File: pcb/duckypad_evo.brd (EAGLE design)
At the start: 90 x 96 mm, 93 parts, among them IC1 STM32F072C8T6, IC2 REG1117, IC3 74AHCT1G08DBV, SW1 324_SW324_SWITCH_FOOT_HOLE, SW10 KAILH_SWITCH_SOCKET_KAILH_SWI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, SW11 KAILH_SWITCH_SOCKET_KAILH_SWI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, SW12 KAILH_SWITCH_SOCKET_KAILH_SWI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, SW13 KAILH_SWITCH_SOCKET_KAILH_SWI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, SW14 KAILH_SWITCH_SOCKET_KAILH_SWI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, SW15 KAILH_SWITCH_SOCKET_KAILH_SWI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

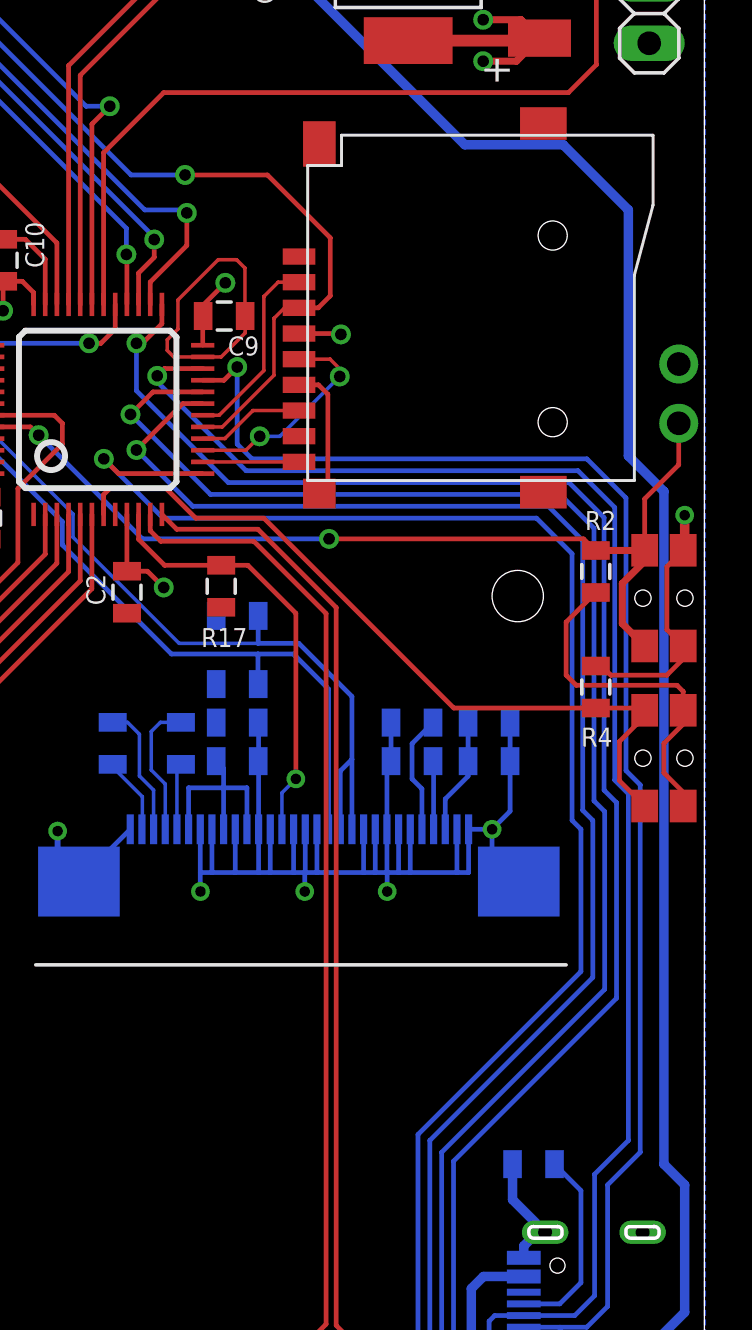
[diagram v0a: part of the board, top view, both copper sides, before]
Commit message: new side-push buttons, new bugfix firmware
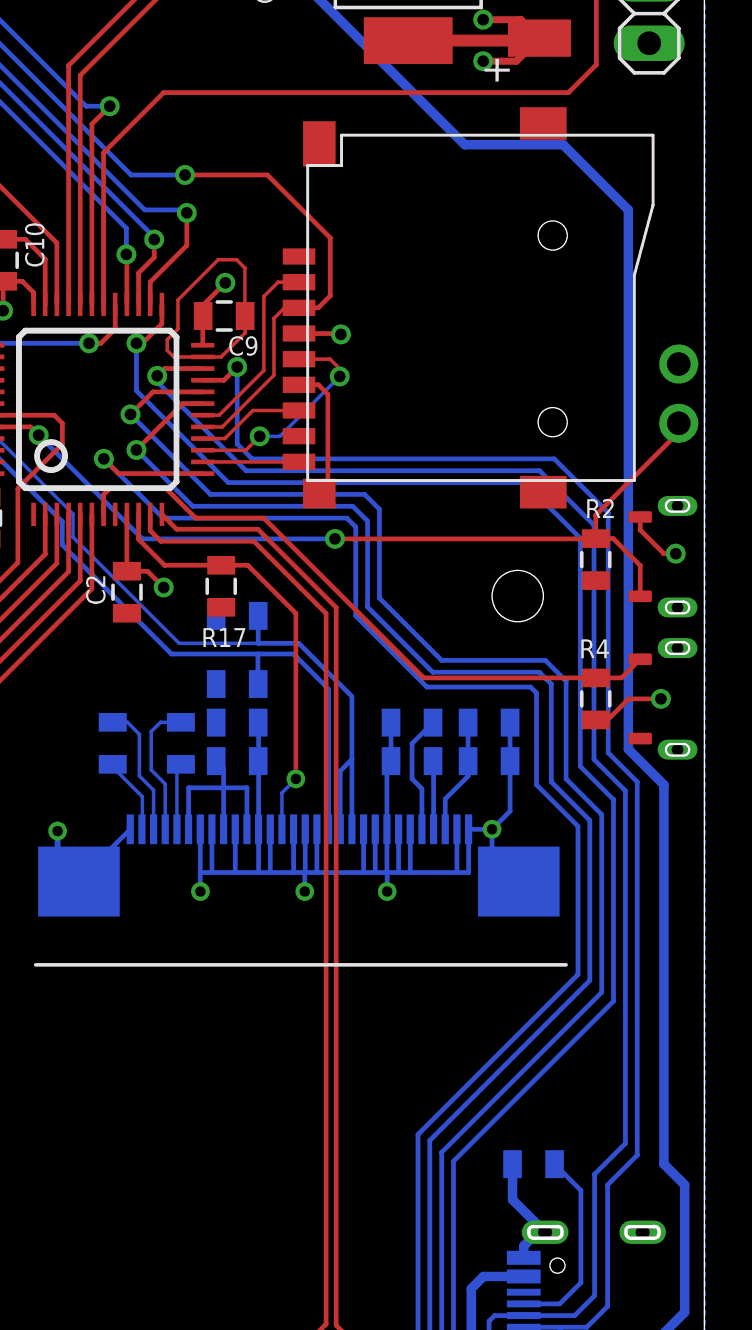
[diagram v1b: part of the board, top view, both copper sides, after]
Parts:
- removed SW1, SW2: 324_SW324_SWITCH_FOOT_HOLE, 3pos_slide_switch:342_SWICH_FOOT_HOLE
- added SW3, SW4: 3POS_SLIDE_SWITCH_324_SW, duckypad:SIDEPUSH
- moved R2 0.51 mm to (85.3, 59.6)
- moved R4 0.51 mm to (85.3, 53.6), turned to 270 degrees
- turned U$14 to 90 degrees
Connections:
- net +3V3: now also SW4.P$1, U$14.2; no longer SW1.P$1, SW1.P$4, U$14.1
- net BUTTON_DEBUG: now also SW4.P$2, U$14.1; no longer SW1.P$2, SW1.P$3, U$14.2
- net GND: now also SW3.GND1, SW3.GND2, SW3.P$2, SW4.GND1, SW4.GND2; no longer SW2.P$2, SW2.P$3
- net RST: now also SW3.P$1; no longer SW2.P$1, SW2.P$4
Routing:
- net GND: track 182.9 -> 167.9 mm
- net RST: track 33.1 -> 27.6 mm
- net +3V3: track 104.5 -> 99.2 mm, vias 8 -> 9
- net BUTTON_DEBUG: track 41.1 -> 38.0 mm
- net N$2: track 82.0 -> 79.6 mm
- net N$13: track 81.7 -> 79.3 mm
- net N$37: track 84.3 -> 82.1 mm
- net N$35: track 82.2 -> 81.0 mm
- net N$16: track 65.9 -> 64.8 mm
- net N$30: track 64.5 -> 63.6 mm
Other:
- board text added: "dekuNukem 2026"
- board text removed: "dekuNukem 2024"
